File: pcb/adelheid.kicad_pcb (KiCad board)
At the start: 2 copper layers, 339.1 x 143.2 mm, 295 parts, among them J1 USB_C_Receptacle_HRO_TYPE-C-3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, J2 Conn_01x06, J3 Conn_01x06, Q1 2N7002, U1 USBLC6-2SC6, U2 ATmega32U4-AU, Y1 Crystal_GND24

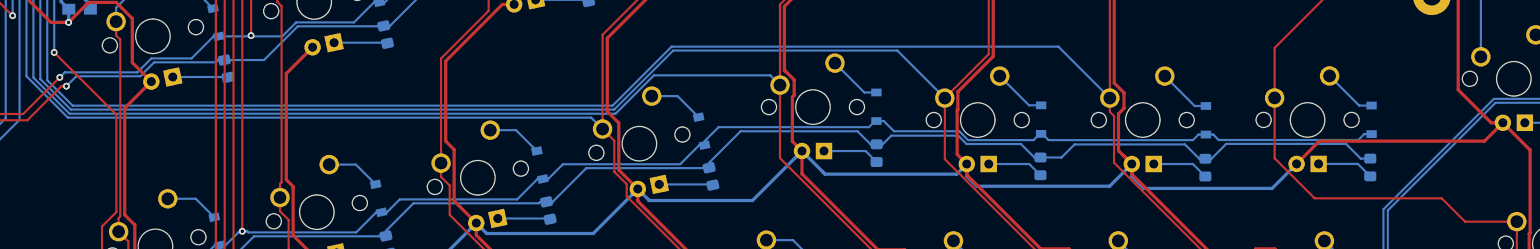
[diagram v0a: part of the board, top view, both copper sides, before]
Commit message: Add a couple of via to clean up a couple gaps in the ground plane
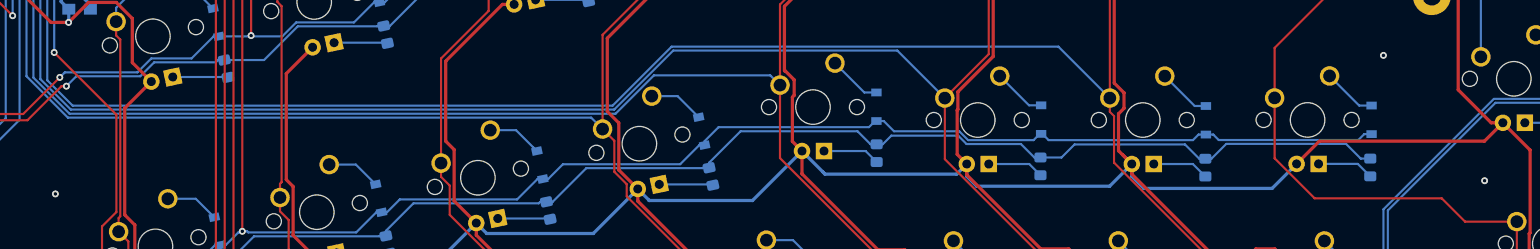
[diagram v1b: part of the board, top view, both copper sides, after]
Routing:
- net GND: vias 4 -> 7
